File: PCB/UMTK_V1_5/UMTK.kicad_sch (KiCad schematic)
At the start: 0 parts

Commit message: Put in Files for V1
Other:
- removed sheet User Interface
- added sheet 7Seg_Display (S1_7Seg_Display.kicad_sch)
- added sheet HX711 (S4_HX711.kicad_sch)

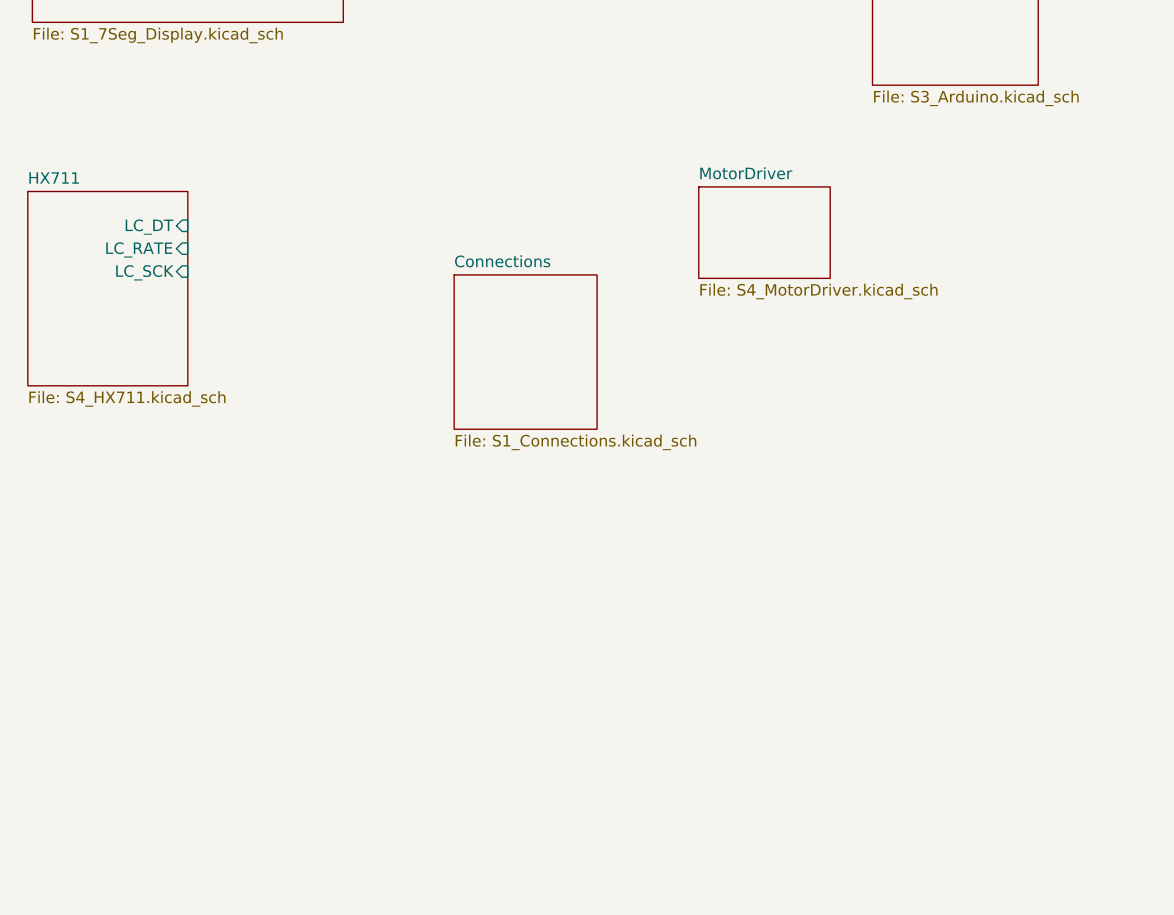
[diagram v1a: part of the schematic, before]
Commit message: Updated Schematics
Done: 7 Seg, Power, Motor, Slide, HX711
To Do: Arduino
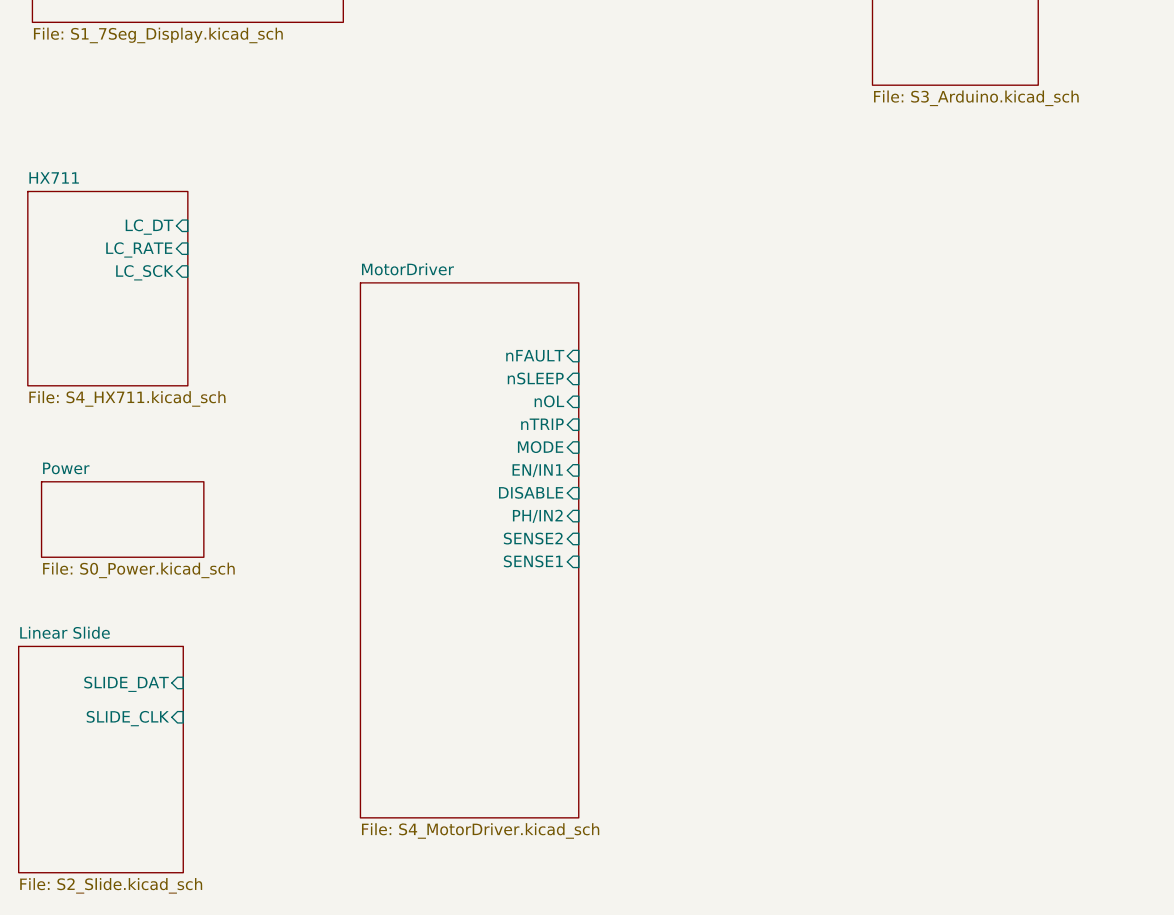
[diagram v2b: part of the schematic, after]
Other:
- removed sheet Connections
- added sheet Linear Slide (S2_Slide.kicad_sch)
- added sheet Power (S0_Power.kicad_sch)
- sheet MotorDriver ports: added DISABLE, EN/IN1, MODE, PH/IN2, SENSE1, SENSE2, nFAULT, nOL, nSLEEP, nTRIP; removed none
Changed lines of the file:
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@@
 	(paper "A4")
 	(sheet
-		(at 66.421 58.547)
-		(size 15.875 17.145)
-		(fields_autoplaced yes)
-		(stroke
-			(width 0.1524)
-			(type solid)
-		)
-		(fill
-			(color 0 0 0 0.0000)
-		)
-		(property "Sheetname" "Connections"
-			(at 66.421 57.8354 0)
-			(effects
-				(font
-					(size 1.27 1.27)
-				)
-				(justify left bottom)
-			)
-		)
-		(property "Sheetfile" "S1_Connections.kicad_sch"
-			(at 66.421 76.2766 0)
-			(effects
-				(font
-					(size 1.27 1.27)
-				)
-				(justify left top)
-			)
-		)
-		(instances
-			(project "UMTK"
-				(path "/2bf3ea67-58b8-47b3-a768-ea6950b40edf"
-					(page "5")
+		(at 18.034 99.822)
+		(size 18.288 25.146)
+		(fields_autoplaced yes)
+		(stroke
+			(width 0.1524)
+			(type solid)
+		)
+		(fill
+			(color 0 0 0 0.0000)
+		)
+		(property "Sheetname" "Linear Slide"
+			(at 18.034 99.1104 0)
+			(effects
+				(font
+					(size 1.27 1.27)
+				)
+				(justify left bottom)
+			)
+		)
+		(property "Sheetfile" "S2_Slide.kicad_sch"
+			(at 18.034 125.5526 0)
+			(effects
+				(font
+					(size 1.27 1.27)
+				)
+				(justify left top)
+			)
+		)
+		(pin "SLIDE_DAT" input
+			(at 36.322 103.886 0)
+			(effects
+				(font
+					(size 1.27 1.27)
+				)
+				(justify right)
+			)
+		)
+		(pin "SLIDE_CLK" input
+			(at 36.322 107.696 0)
+			(effects
+				(font
+					(size 1.27 1.27)
+				)
+				(justify right)
+			)
+		)
+		(instances
+			(project "UMTK"
+				(path "/2bf3ea67-58b8-47b3-a768-ea6950b40edf"
+					(page "8")
 				)
 			)
@@
 	)
 	(sheet
-		(at 93.599 48.768)
-		(size 14.605 10.16)
+		(at 56.007 59.436)
+		(size 24.257 59.436)
 		(fields_autoplaced yes)
 		(stroke
@@
 		)
 		(property "Sheetname" "MotorDriver"
-			(at 93.599 48.0564 0)
+			(at 56.007 58.7244 0)
 			(effects
 				(font
@@
 		)
 		(property "Sheetfile" "S4_MotorDriver.kicad_sch"
-			(at 93.599 59.5126 0)
-			(effects
-				(font
-					(size 1.27 1.27)
-				)
-				(justify left top)
+			(at 56.007 119.4566 0)
+			(effects
+				(font
+					(size 1.27 1.27)
+				)
+				(justify left top)
+			)
+		)
+		(pin "nFAULT" input
+			(at 80.264 67.564 0)
+			(effects
+				(font
+					(size 1.27 1.27)
+				)
+				(justify right)
+			)
+		)
+		(pin "nSLEEP" input
+			(at 80.264 70.104 0)
+			(effects
+				(font
+					(size 1.27 1.27)
+				)
+				(justify right)
+			)
+		)
+		(pin "nOL" input
+			(at 80.264 72.644 0)
+			(effects
+				(font
+					(size 1.27 1.27)
+				)
+				(justify right)
+			)
+		)
+		(pin "nTRIP" input
+			(at 80.264 75.184 0)
+			(effects
+				(font
+					(size 1.27 1.27)
+				)
+				(justify right)
+			)
+		)
+		(pin "MODE" input
+			(at 80.264 77.724 0)
+			(effects
+				(font
+					(size 1.27 1.27)
+				)
+				(justify right)
+			)
+		)
+		(pin "EN{slash}IN1" input
+			(at 80.264 80.264 0)
+			(effects
+				(font
+					(size 1.27 1.27)
+				)
+				(justify right)
+			)
+		)
+		(pin "DISABLE" input
+			(at 80.264 82.804 0)
+			(effects
+				(font
+					(size 1.27 1.27)
+				)
+				(justify right)
+			)
+		)
+		(pin "PH{slash}IN2" input
+			(at 80.264 85.344 0)
+			(effects
+				(font
+					(size 1.27 1.27)
+				)
+				(justify right)
+			)
+		)
+		(pin "SENSE2" input
+			(at 80.264 87.884 0)
+			(effects
+				(font
+					(size 1.27 1.27)
+				)
+				(justify right)
+			)
+		)
+		(pin "SENSE1" input
+			(at 80.264 90.424 0)
+			(effects
+				(font
+					(size 1.27 1.27)
+				)
+				(justify right)
 			)
 		)
@@
 				)
 			)
+		)
+	)
+	(sheet
+		(at 20.574 81.534)
+		(size 18.034 8.382)
+		(fields_autoplaced yes)
+		(stroke
+			(width 0.1524)
+			(type solid)
+		)
+		(fill
+			(color 0 0 0 0.0000)
+		)
+		(property "Sheetname" "Power"
+			(at 20.574 80.8224 0)
+			(effects
+				(font
+					(size 1.27 1.27)
+				)
+				(justify left bottom)
+			)
+		)
+		(property "Sheetfile" "S0_Power.kicad_sch"
+			(at 20.574 90.5006 0)
+			(effects
+				(font
+					(size 1.27 1.27)
+				)
+				(justify left top)
+			)
+		)
+		(instances
+			(project "UMTK"
+				(path "/2bf3ea67-58b8-47b3-a768-ea6950b40edf"
+					(page "7")
+				)
+			)

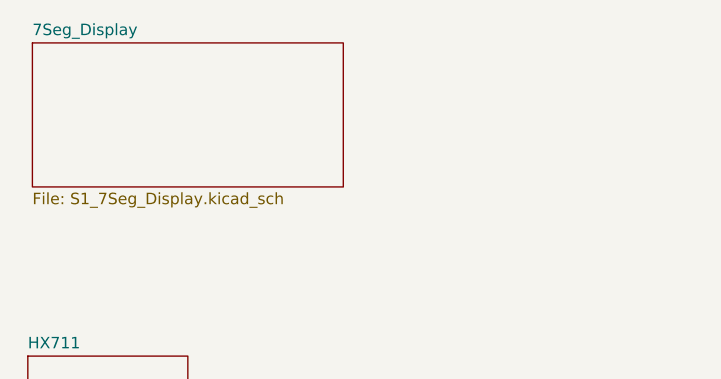
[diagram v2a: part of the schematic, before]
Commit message: Export Subsheet Pin From 7Seg
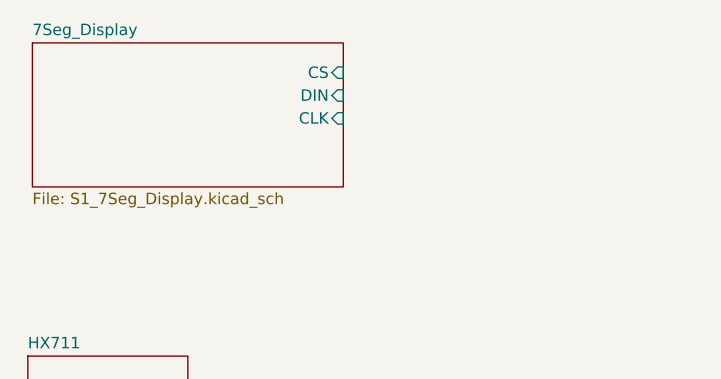
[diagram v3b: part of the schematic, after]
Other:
- sheet 7Seg_Display ports: added CLK, CS, DIN; removed none
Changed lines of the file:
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@@
+			)
+		)
+		(pin "CS" input
+			(at 54.102 17.78 0)
+			(effects
+				(font
+					(size 1.27 1.27)
+				)
+				(justify right)
+			)
+		)
+		(pin "DIN" input
+			(at 54.102 20.32 0)
+			(effects
+				(font
+					(size 1.27 1.27)
+				)
+				(justify right)
+			)
+		)
+		(pin "CLK" input
+			(at 54.102 22.86 0)
+			(effects
+				(font
+					(size 1.27 1.27)
+				)
+				(justify right)
 			)
 		)

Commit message: Updating Schematic
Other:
- sheet Arduino ports: added 7SEG_CLK, 7SEG_CS, 7SEG_DIN, LC_DT, LC_RATE, LC_SCK, MOT_DISABLE, MOT_EN_N1, MOT_MODE, MOT_PH_IN2, MOT_SENSE1, MOT_SENSE2, MOT_nFAULT, MOT_nITRIP, MOT_nOL, MOT_nSLEEP, SLIDE_CLK, SLIDE_DAT; removed none
- sheet MotorDriver ports: added nITRIP; removed nTRIP

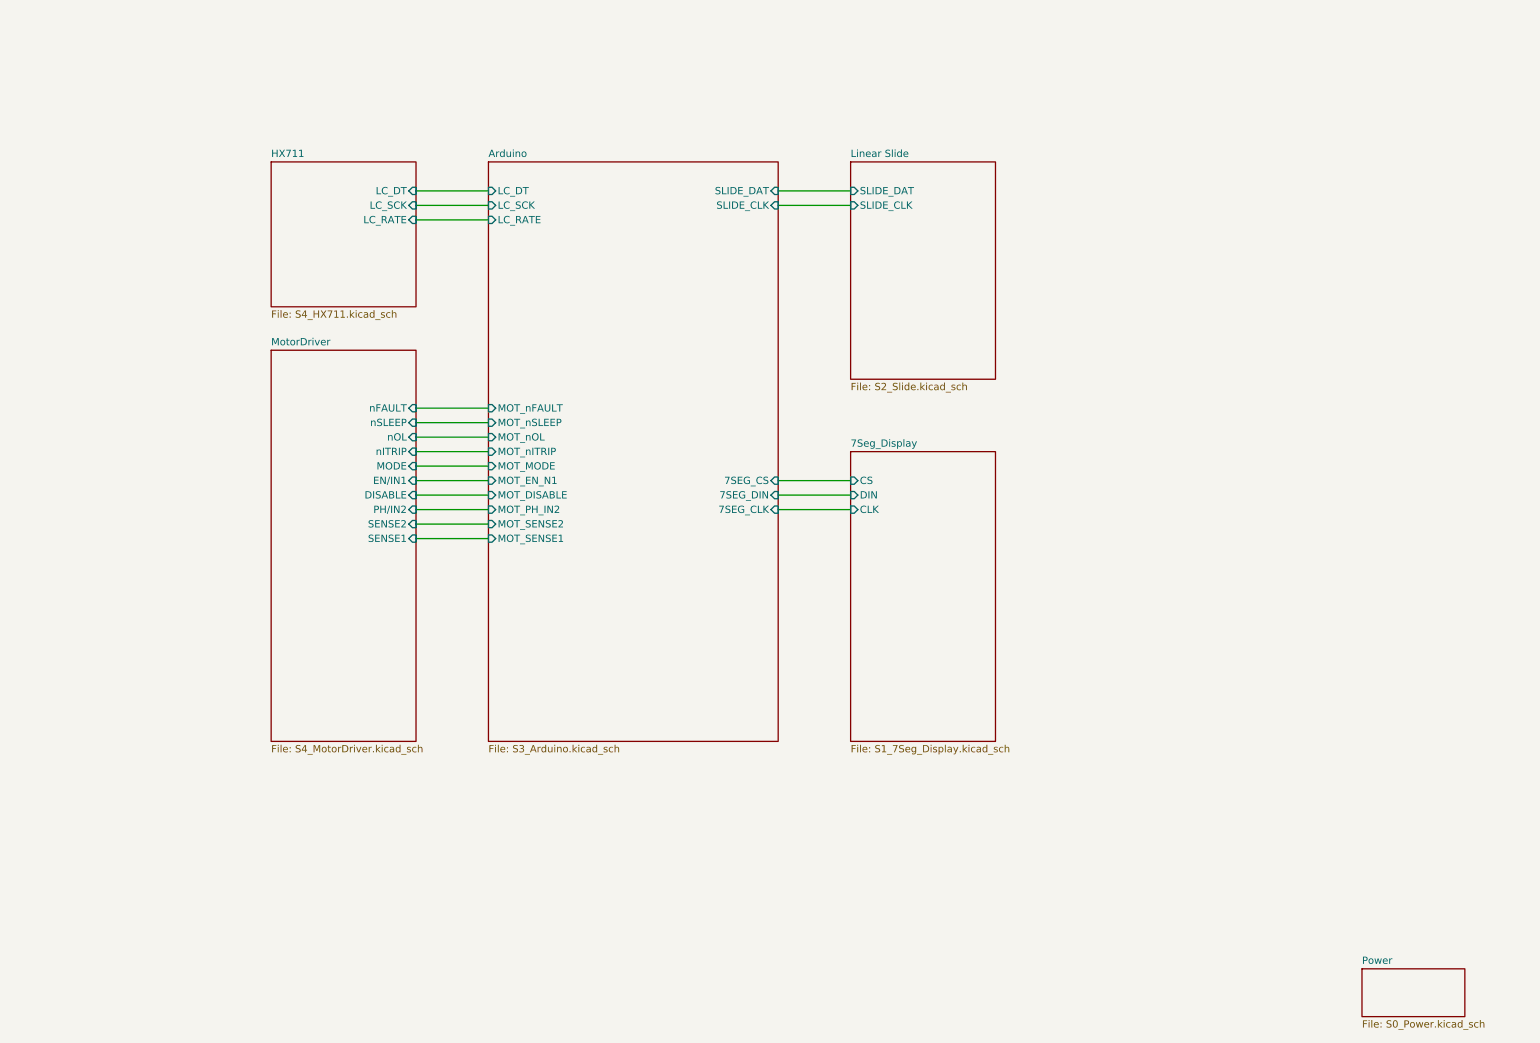
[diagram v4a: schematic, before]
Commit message: Schematic Done, Assigning footprint
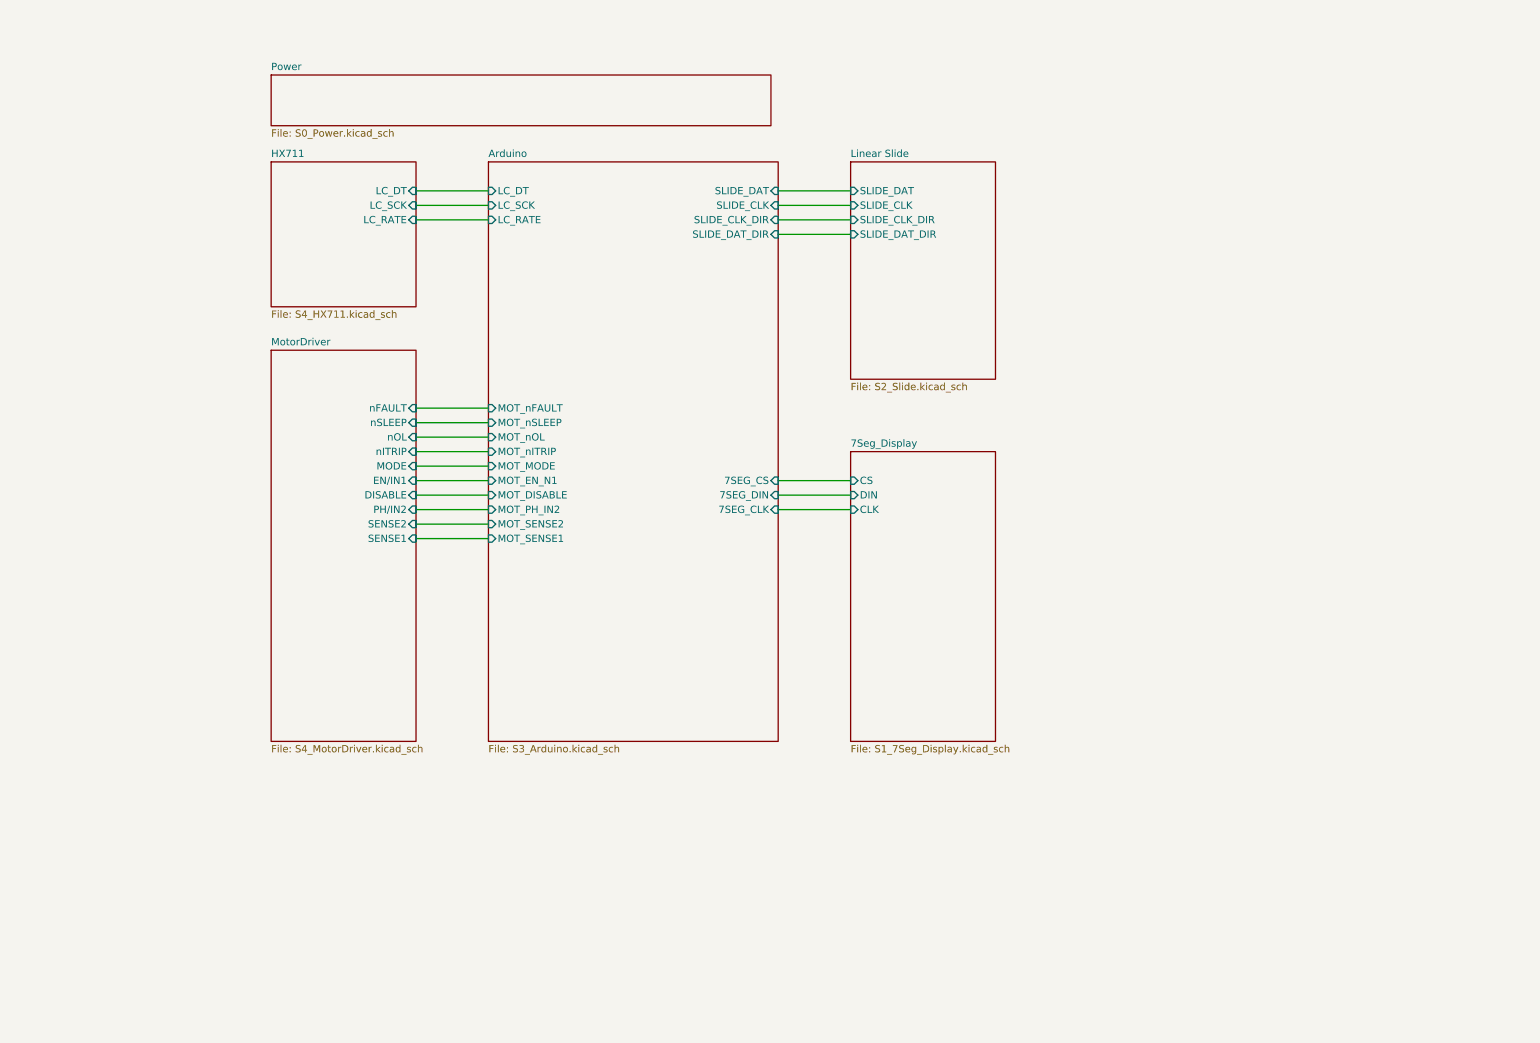
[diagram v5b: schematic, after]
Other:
- sheet Arduino ports: added SLIDE_CLK_DIR, SLIDE_DAT_DIR; removed none
- sheet Linear Slide ports: added SLIDE_CLK_DIR, SLIDE_DAT_DIR; removed none
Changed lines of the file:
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@@
+	(wire
+		(pts
+			(xy 152.4 50.8) (xy 165.1 50.8)
+		)
+		(stroke
+			(width 0)
+			(type default)
+		)
+	)
 	(wire
 		(pts
@@
 		(pts
 			(xy 152.4 43.18) (xy 165.1 43.18)
+		)
+		(stroke
+			(width 0)
+			(type default)
+		)
+	)
+	(wire
+		(pts
+			(xy 152.4 48.26) (xy 165.1 48.26)
 		)
 		(stroke
@@
 			)
 		)
+		(pin "SLIDE_CLK_DIR" input
+			(at 165.1 48.26 180)
+			(effects
+				(font
+					(size 1.27 1.27)
+				)
+				(justify left)
+			)
+		)
+		(pin "SLIDE_DAT_DIR" input
+			(at 165.1 50.8 180)
+			(effects
+				(font
+					(size 1.27 1.27)
+				)
+				(justify left)
+			)
+		)
 		(instances
 			(project "UMTK"
@@
 			)
 		)
+		(pin "SLIDE_CLK_DIR" input
+			(at 152.4 48.26 0)
+			(effects
+				(font
+					(size 1.27 1.27)
+				)
+				(justify right)
+			)
+		)
+		(pin "SLIDE_DAT_DIR" input
+			(at 152.4 50.8 0)
+			(effects
+				(font
+					(size 1.27 1.27)
+				)
+				(justify right)
+			)
+		)
 		(instances
 			(project "UMTK"
@@
 	)
 	(sheet
-		(at 254.762 179.578)
-		(size 18.034 8.382)
+		(at 63.5 22.86)
+		(size 87.63 8.89)
 		(fields_autoplaced yes)
 		(stroke
@@
 		)
 		(property "Sheetname" "Power"
-			(at 254.762 178.8664 0)
+			(at 63.5 22.1484 0)
 			(effects
 				(font
@@
 		)
 		(property "Sheetfile" "S0_Power.kicad_sch"
-			(at 254.762 188.5446 0)
-			(effects
-				(font
+			(at 63.5 32.3346 0)
+			(effects
+				(font

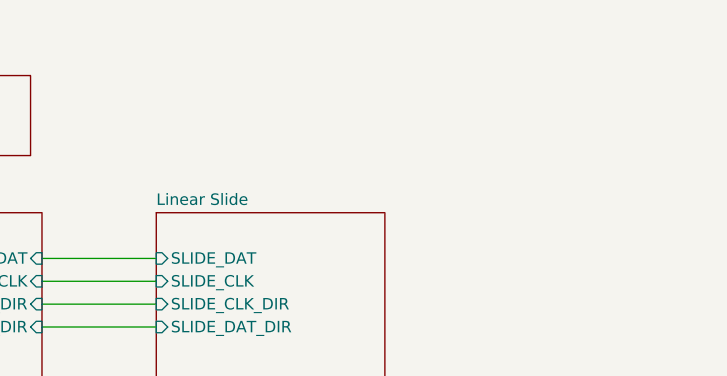
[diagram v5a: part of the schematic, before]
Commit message: Placement Approved, Added holes
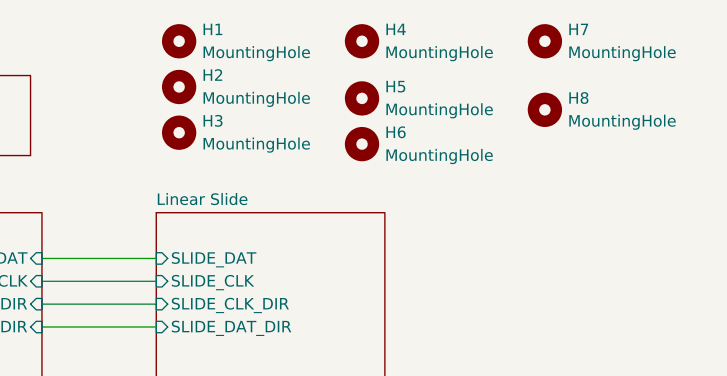
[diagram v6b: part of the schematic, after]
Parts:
- added H1, H2, H3, H4, H5, H6, H7, H8: MountingHole, MountingHole:MountingHole_4mm, symbol Mechanical:MountingHole

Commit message: Routing
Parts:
- added H9: MountingHole, MountingHole:MountingHole_4mm, symbol Mechanical:MountingHole
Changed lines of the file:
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@@
+	(symbol
+		(lib_id "Mechanical:MountingHole")
+		(at 208.28 33.02 0)
+		(unit 1)
+		(exclude_from_sim yes)
+		(in_bom no)
+		(on_board yes)
+		(dnp no)
+		(fields_autoplaced yes)
+		(property "Reference" "H9"
+			(at 210.82 31.7499 0)
+			(effects
+				(font
+					(size 1.27 1.27)
+				)
+				(justify left)
+			)
+		)
+		(property "Value" "MountingHole"
+			(at 210.82 34.2899 0)
+			(effects
+				(font
+					(size 1.27 1.27)
+				)
+				(justify left)
+			)
+		)
+		(property "Footprint" "MountingHole:MountingHole_4mm"
+			(at 208.28 33.02 0)
+			(effects
+				(font
+					(size 1.27 1.27)
+				)
+				(hide yes)
+			)
+		)
+		(property "Datasheet" "~"
+			(at 208.28 33.02 0)
+			(effects
+				(font
+					(size 1.27 1.27)
+				)
+				(hide yes)
+			)
+		)
+		(property "Description" "Mounting Hole without connection"
+			(at 208.28 33.02 0)
+			(effects
+				(font
+					(size 1.27 1.27)
+				)
+				(hide yes)
+			)
+		)
+		(instances
+			(project "UMTK"
+				(path "/2bf3ea67-58b8-47b3-a768-ea6950b40edf"
+					(reference "H9")
+					(unit 1)
+				)
+			)
+		)
+	)
 	(symbol
 		(lib_id "Mechanical:MountingHole")

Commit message: Assigning JLC
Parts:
- added G1: Tensile Cat, AMX_Logo:Tensile Cat, symbol Graphic:SYM_EasterEgg_42x60mm
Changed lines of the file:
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@@
+	)
+	(symbol
+		(lib_id "Graphic:SYM_EasterEgg_42x60mm")
+		(at 229.87 123.19 0)
+		(unit 1)
+		(exclude_from_sim no)
+		(in_bom no)
+		(on_board yes)
+		(dnp no)
+		(fields_autoplaced yes)
+		(property "Reference" "G1"
+			(at 229.87 123.19 0)
+			(effects
+				(font
+					(size 1.27 1.27)
+				)
+				(hide yes)
+			)
+		)
+		(property "Value" "Tensile Cat"
+			(at 229.87 123.19 0)
+			(effects
+				(font
+					(size 1.27 1.27)
+				)
+				(hide yes)
+			)
+		)
+		(property "Footprint" "AMX_Logo:Tensile Cat"
+			(at 229.87 127 0)
+			(effects
+				(font
+					(size 1.27 1.27)
+				)
+				(hide yes)
+			)
+		)
+		(property "Datasheet" "https://eur-lex.europa.eu/LexUriServ/LexUriServ.do?uri=OJ:L:2013:347:0671:0854:de:PDF"
+			(at 229.87 129.54 0)
+			(effects
+				(font
+					(size 1.27 1.27)
+				)
+				(hide yes)
+			)
+		)
+		(property "Description" "EasterEgg, ClassA, Medium Size"
+			(at 229.87 123.19 0)
+			(effects
+				(font
+					(size 1.27 1.27)
+				)
+				(hide yes)
+			)
+		)
+		(property "Sim.Enable" "0"
+			(at 229.87 125.73 0)
+			(effects
+				(font
+					(size 1.27 1.27)
+				)
+				(hide yes)
+			)
+		)
+		(instances
+			(project ""
+				(path "/2bf3ea67-58b8-47b3-a768-ea6950b40edf"
+					(reference "G1")
+					(unit 1)
+				)
+			)
+		)
 	)
 	(symbol
